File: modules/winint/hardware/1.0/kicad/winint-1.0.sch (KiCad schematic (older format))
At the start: 39 parts, among them J1 NPN SENSOR, J2 Screw_Terminal_01x05, J3 M12-5PIN, J4 RELAYS, K1 SANYOU_SRD_Form_C, K2 SANYOU_SRD_Form_C, Q1 2N2219, Q2 2N2219, SW1 INSTANCE, U1 CNY74-4H, U2 Teensy_3.2, U3 TEC2-2411WI, U4 MCP2551-I-P

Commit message: Refactor again
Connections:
- net at R8.1: now also U2.10 (D8/TX3); no longer U2.12 (D10/TX2)
- net at U1.15: now also U2.11 (D9/RX2); no longer U2.10 (D8/TX3)
- net at U1.14: now also U2.12 (D10/TX2); no longer U2.11 (D9/RX2)
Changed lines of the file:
@@
 	5750 2800 5450 2800
 Wire Wire Line
-	5450 2800 5450 1550
-Wire Wire Line
-	5450 1550 5050 1550
+	5450 2800 5450 1750
 Connection ~ 5150 3000
 $Comp
@@
 	2450 850  2450 3350
 Wire Wire Line
-	5550 1750 5050 1750
-Wire Wire Line
-	5550 850  5550 1750
-Wire Wire Line
-	5350 1650 5050 1650
-Wire Wire Line
-	5350 950  5350 1650
+	5550 850  5550 1650
+Wire Wire Line
+	5350 950  5350 1550
 Wire Wire Line
 	5050 1450 5250 1450
@@
 Wire Wire Line
 	9500 4950 9600 4950
+Wire Wire Line
+	5050 1550 5350 1550
+Wire Wire Line
+	5050 1650 5550 1650
+Wire Wire Line
+	5050 1750 5450 1750
 $EndSCHEMATC

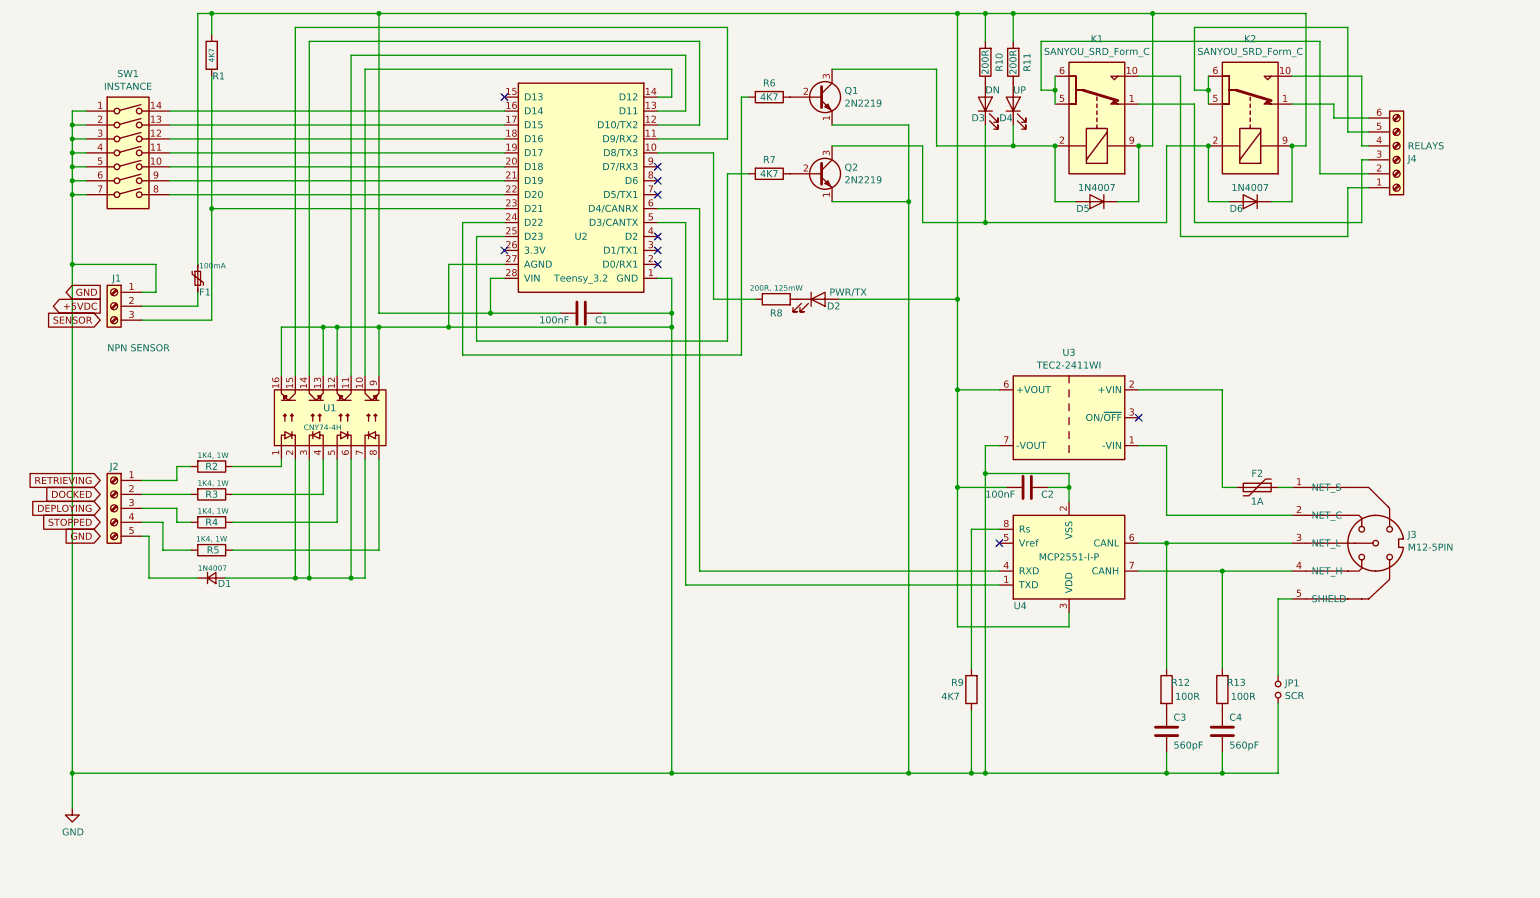
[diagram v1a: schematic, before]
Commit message: Added 12V fused supply and OPTO isolation to rotation sensor input
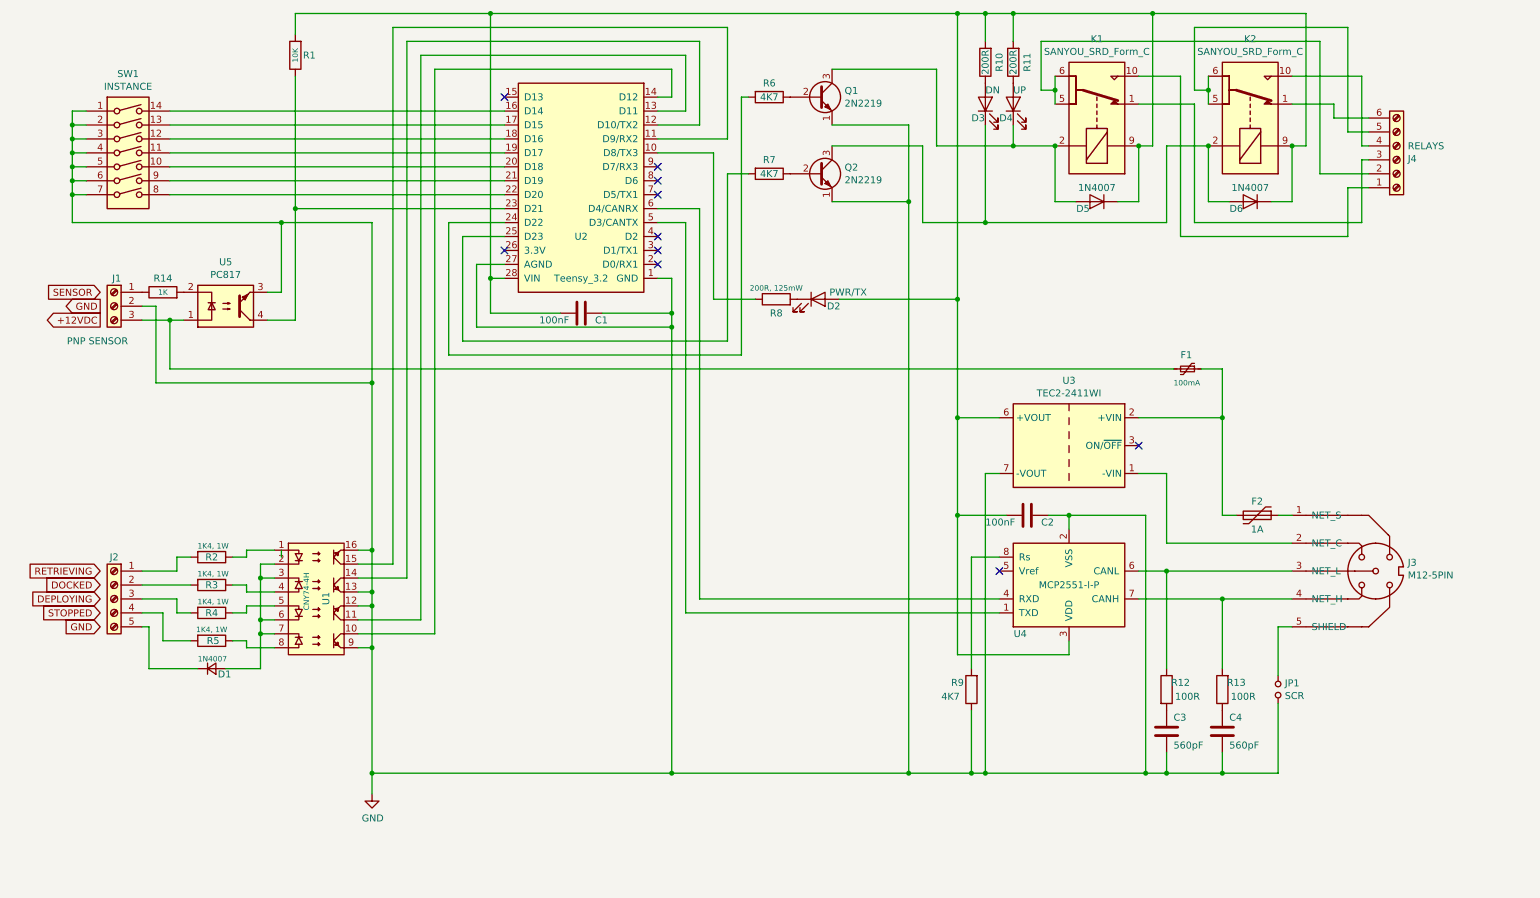
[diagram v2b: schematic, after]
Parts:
- added R14: 1K, Resistor_THT:R_Axial_DIN0204_L3.6mm_D1.6mm_P5.08mm_Horizontal, symbol Device:R
- added U5: PC817, Package_DIP:DIP-4_W7.62mm, symbol Isolator:PC817
- J1: value NPN SENSOR -> PNP SENSOR
- R1: value 4K7 -> 10K
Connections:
- net GND: now also J1.2 (Pin_2), U5.3; no longer J1.1 (Pin_1)
- net at F1.2: now also J1.3 (Pin_3), U5.1; no longer J1.2 (Pin_2)
- net at R1.1, U2.23 (D21): now also U5.4; no longer J1.3 (Pin_3)
- net at C1.1, C2.1, D2.2 (A)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: no longer F1.1
- net at F2.2, U3.2 (+VIN): now also F1.1
- new net: J1.1 (Pin_1), R14.1
- new net: R14.2, U5.2
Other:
- moved on the sheet: C2, D1, F1, F2, J2, J3, R1, R2, R3, R4, R5, U1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

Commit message: Added 12V fused supply and OPTO isolation to rotation sensor input
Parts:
- D2, D3, D4: footprint LED_THT:LED_Rectangular_W3.0mm_H2.0mm -> LED_THT:LED_D3.0mm
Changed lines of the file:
@@
 F 0 "D4" V 7500 1500 50  0000 R CNN
 F 1 "UP" V 7700 1400 50  0000 R CNN
-F 2 "LED_THT:LED_Rectangular_W3.0mm_H2.0mm" H 7600 1400 50  0001 C CNN
+F 2 "LED_THT:LED_D3.0mm" H 7600 1400 50  0001 C CNN
 F 3 "~" H 7600 1400 50  0001 C CNN
 	1    7600 1400
@@
 F 0 "D3" V 7300 1500 50  0000 R CNN
 F 1 "DN" V 7500 1400 50  0000 R CNN
-F 2 "LED_THT:LED_Rectangular_W3.0mm_H2.0mm" H 7400 1400 50  0001 C CNN
+F 2 "LED_THT:LED_D3.0mm" H 7400 1400 50  0001 C CNN
 F 3 "~" H 7400 1400 50  0001 C CNN
 	1    7400 1400
@@
 F 0 "D2" H 6360 2750 50  0000 R CNN
 F 1 "PWR/TX" H 6550 2850 50  0000 R CNN
-F 2 "LED_THT:LED_Rectangular_W3.0mm_H2.0mm" H 6200 2800 50  0001 C CNN
+F 2 "LED_THT:LED_D3.0mm" H 6200 2800 50  0001 C CNN
 F 3 "~" H 6200 2800 50  0001 C CNN
 	1    6200 2800

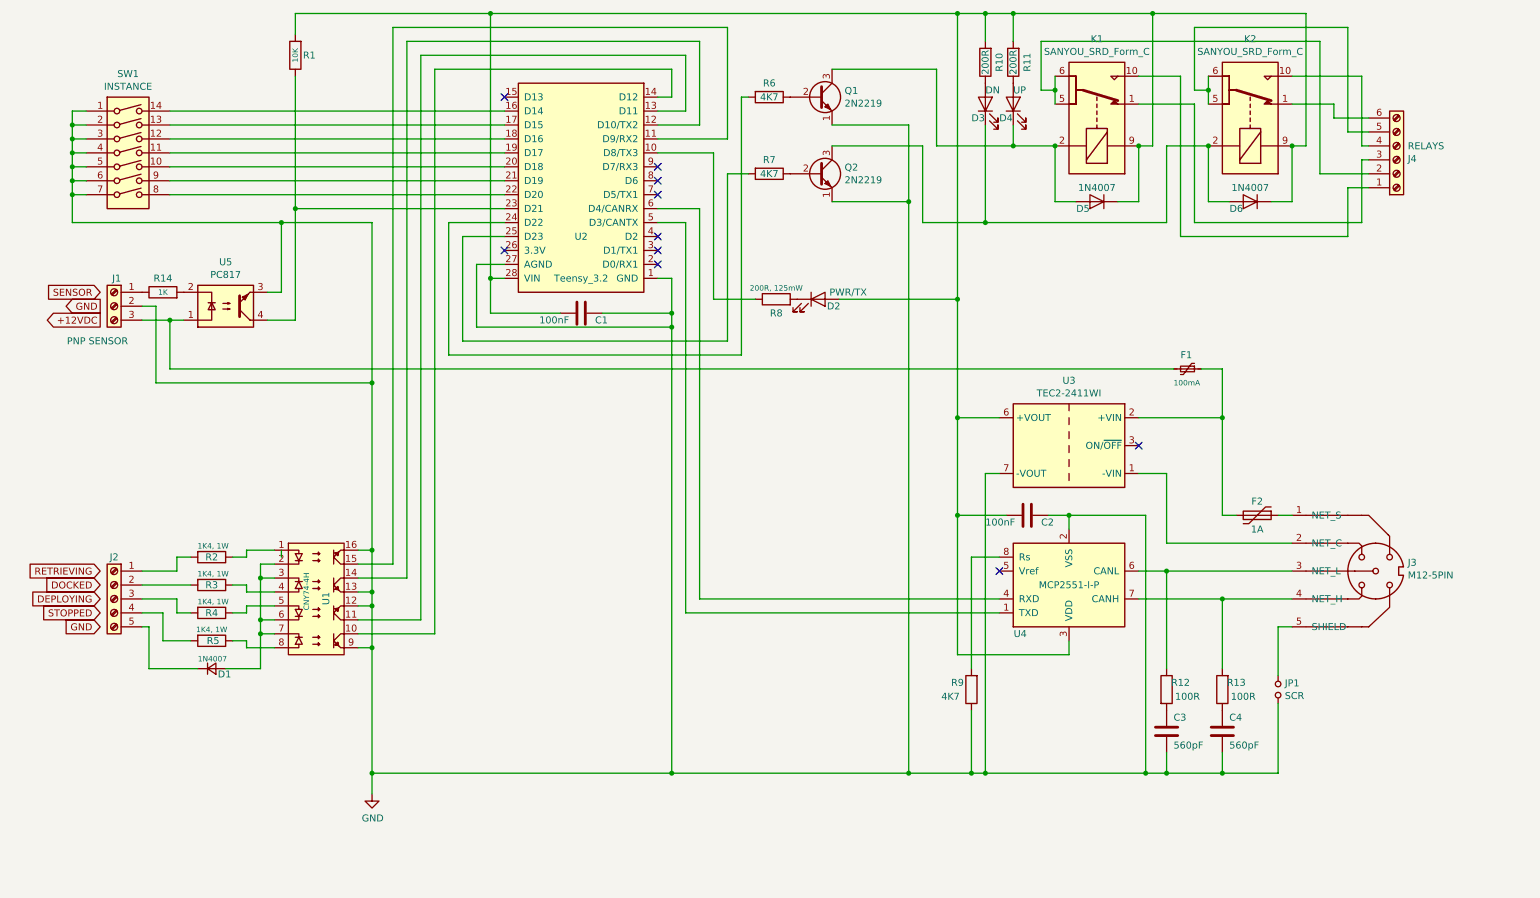
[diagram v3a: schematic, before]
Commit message: Revised for mult-mode inputs
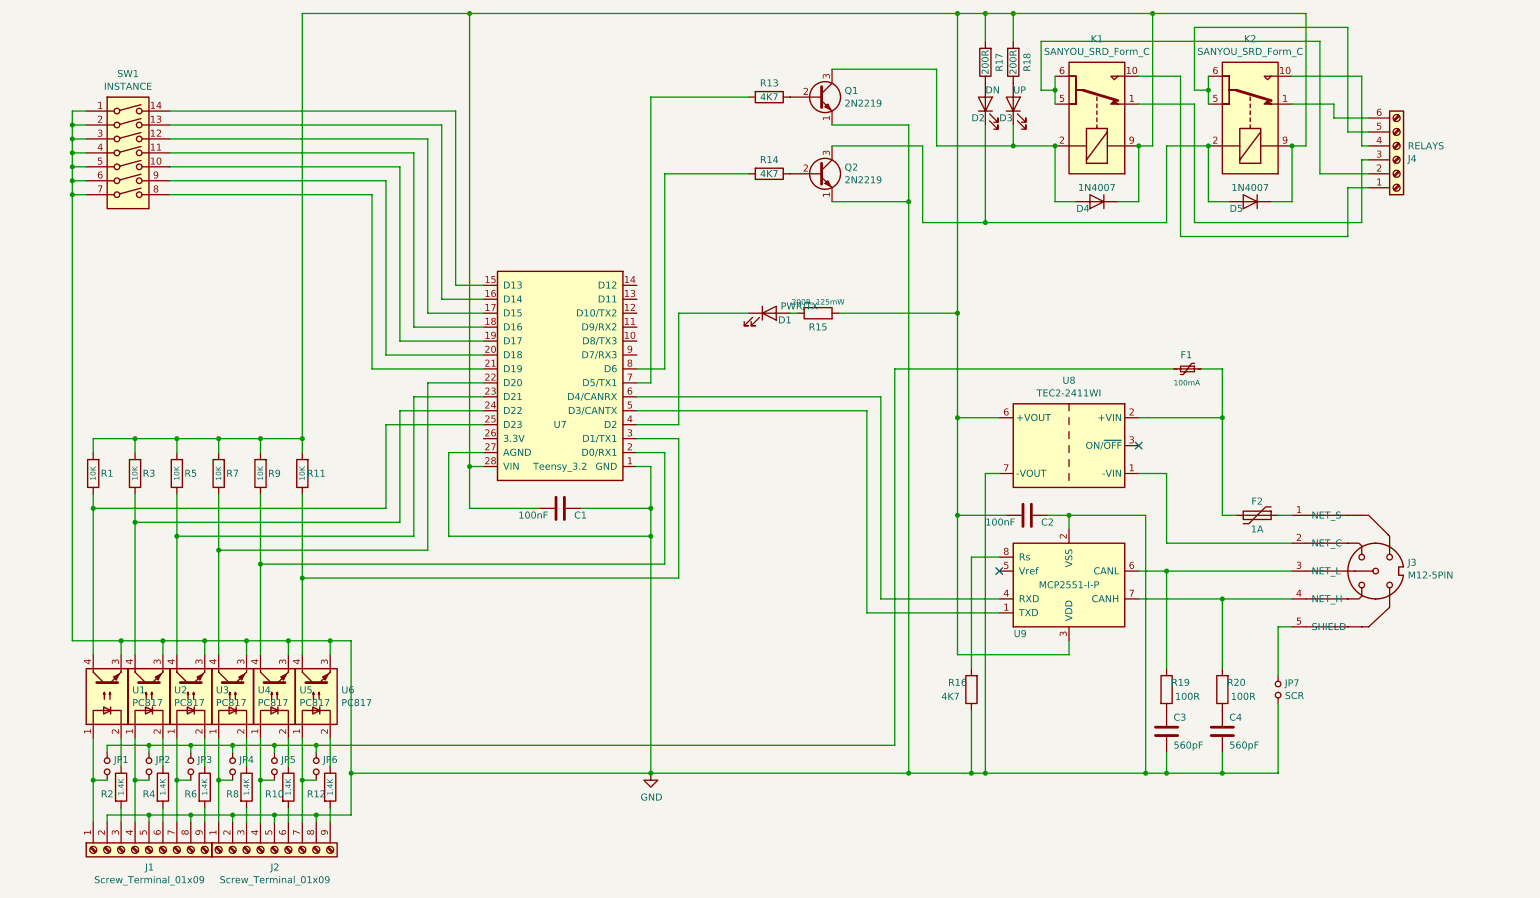
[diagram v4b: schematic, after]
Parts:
- removed D1: 1N4007, Diode_THT:D_DO-35_SOD27_P2.54mm_Vertical_AnodeUp, symbol Device:D_Small
- removed J1: PNP SENSOR, PDJR:TerminalBlock_Phoenix_MPT-0,5-3-2.54_1x03_P2.54mm_Horizontal, symbol Connector:Screw_Terminal_01x03
- removed J2: Screw_Terminal_01x05, TerminalBlock_Phoenix:TerminalBlock_Phoenix_MPT-0,5-5-2.54_1x05_P2.54mm_Horizontal, symbol Connector:Screw_Terminal_01x05
- removed R14: 1K, Resistor_THT:R_Axial_DIN0204_L3.6mm_D1.6mm_P5.08mm_Horizontal, symbol Device:R
- removed U1: CNY74-4H, Package_DIP:DIP-16_W7.62mm_LongPads, symbol pdjr:CNY74-4H
- added J1, J2: Screw_Terminal_01x09, TerminalBlock_Phoenix:TerminalBlock_Phoenix_MPT-0,5-9-2.54_1x09_P2.54mm_Horizontal, symbol Connector:Screw_Terminal_01x09
- added JP1, JP2, JP3, JP4, JP5, JP6: SCR, Connector_PinHeader_2.54mm:PinHeader_1x02_P2.54mm_Vertical, symbol Device:Jumper_NO_Small
- added R10, R12, R6, R8: 1.4K, Resistor_THT:R_Axial_DIN0204_L3.6mm_D1.6mm_P5.08mm_Horizontal, symbol Device:R
- added R11, R7, R9: 10K, Resistor_THT:R_Axial_DIN0204_L3.6mm_D1.6mm_P5.08mm_Horizontal, symbol Device:R
- added U1, U2, U3, U4, U6: PC817, Package_DIP:DIP-4_W7.62mm, symbol Isolator:PC817
- R2, R4: value 1K4, 1W -> 1.4K; footprint Resistor_THT:R_Axial_DIN0207_L6.3mm_D2.5mm_P2.54mm_Vertical -> Resistor_THT:R_Axial_DIN0204_L3.6mm_D1.6mm_P5.08mm_Horizontal
- R3, R5: value 1K4, 1W -> 10K; footprint Resistor_THT:R_Axial_DIN0207_L6.3mm_D2.5mm_P2.54mm_Vertical -> Resistor_THT:R_Axial_DIN0204_L3.6mm_D1.6mm_P5.08mm_Horizontal
- renumbered D2 to D1, D3 to D2, D4 to D3, D5 to D4, D6 to D5, JP1 to JP7, R6 to R13, R7 to R14, R8 to R15, R9 to R16, R10 to R17, R11 to R18, R12 to R19, R13 to R20, U2 to U7, U3 to U8, U4 to U9
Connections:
- net GND: now also J1.2 (Pin_2), J1.5 (Pin_5), J1.8 (Pin_8), J2.2 (Pin_2), J2.5 (Pin_5), J2.8 (Pin_8), U1.3, U2.3, U3.3, U4.3, U6.3
- net at R2.1: now also U1.2
- net at R2.2: now also J1.3 (Pin_3)
- net at F1.2: now also JP1.2, JP2.2, JP3.2, JP4.2, JP5.2, JP6.2; no longer U5.1
- net at C1.1, C2.1, D4.1 (K)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: now also R15.2, R3.2, R5.2, R11.2, R7.2, R9.2; no longer D1.2 (A)
- net at R13.2: now also U7.7 (D5/TX1); no longer U7.24 (D22)
- net at R14.2: now also U7.8 (D6); no longer U7.25 (D23)
- net at R15.1: now also D1.2 (A); no longer U7.10 (D8/TX3)
- net at D1.1 (K): now also U7.4 (D2); no longer R15.2
- net at U7.15 (D13): now also SW1.14
- net at U7.16 (D14): now also SW1.13; no longer SW1.14
- net at U7.17 (D15): now also SW1.12; no longer SW1.13
- net at U7.18 (D16): now also SW1.11; no longer SW1.12
- net at U7.19 (D17): now also SW1.10; no longer SW1.11
- net at U7.2 (D0/RX1): now also U5.4, R9.1
- net at U7.20 (D18): now also SW1.9; no longer SW1.10
- net at U7.21 (D19): now also SW1.8; no longer SW1.9
- net at U7.22 (D20): now also R7.1, U4.4; no longer SW1.8
- net at U7.3 (D1/TX1): now also R11.1, U6.4
- net at R4.2: now also J1.6 (Pin_6)
- net at R3.1: now also U7.24 (D22), U2.4
- net at R4.1: now also U2.2
- net at R5.1: now also U7.23 (D21), U3.4
- net at U5.2: now also R10.1
- new net: R1.1, U1.4, U7.25 (D23)
- new net: J1.1 (Pin_1), JP1.1, U1.1
- new net: J1.4 (Pin_4), JP2.1, U2.1
- new net: J1.7 (Pin_7), JP3.1, U3.1
- new net: J1.9 (Pin_9), R6.2
- new net: J2.1 (Pin_1), JP4.1, U4.1
- new net: J2.3 (Pin_3), R8.2
- new net: J2.4 (Pin_4), JP5.1, U5.1
- new net: J2.6 (Pin_6), R10.2
- new net: J2.7 (Pin_7), JP6.1, U6.1
- new net: J2.9 (Pin_9), R12.2
- new net: R6.1, U3.2
- new net: R8.1, U4.2
- new net: R12.1, U6.2
- no-connect marks 10 -> 2
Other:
- moved on the sheet: C1, D1, R1, R15, U7
